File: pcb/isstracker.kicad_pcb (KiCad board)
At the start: 2 copper layers, 18 parts, among them J1 Display, J2 CONTROL, J3 POWER, J4 Error LED, J5 POWER_OUT, Q1 MMBT2222A, Q2 MMBT2222A, U1 CJT1117-5.0

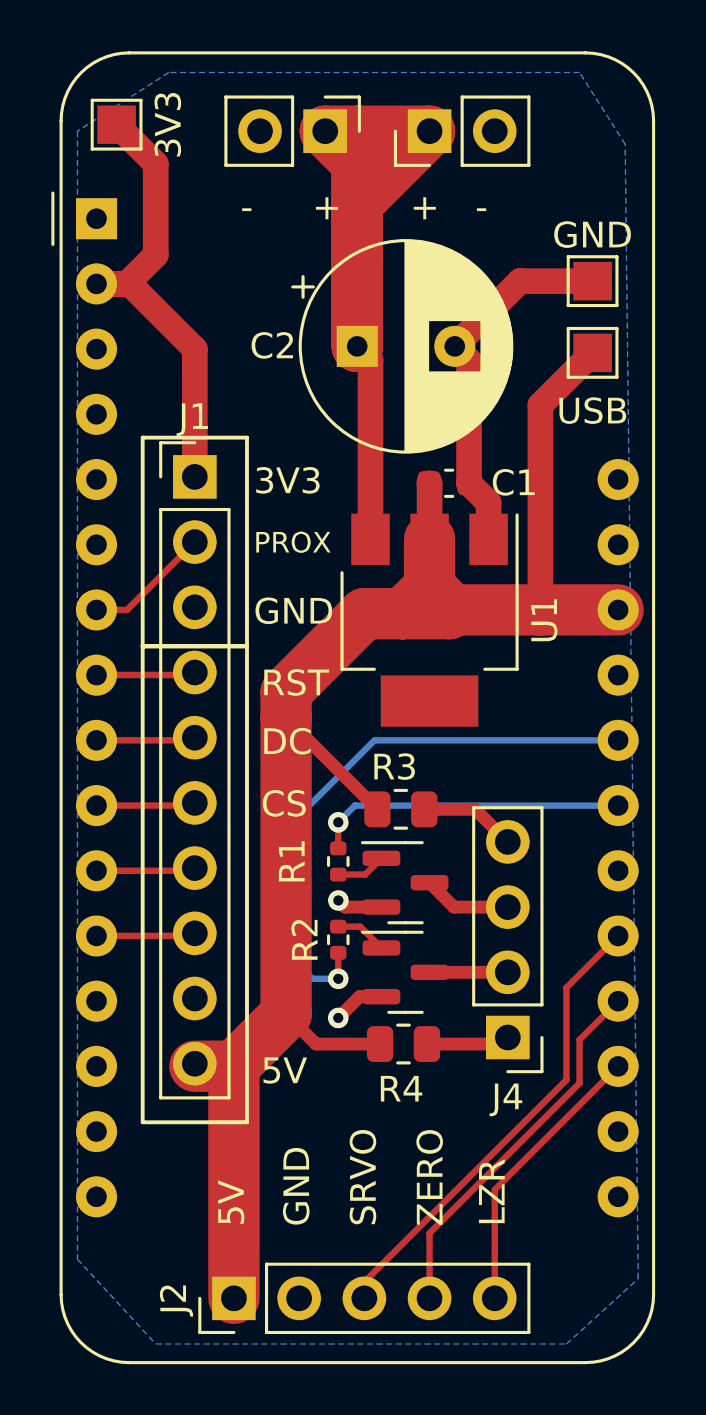
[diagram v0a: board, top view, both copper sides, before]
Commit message: Updating to add internal globe LED control
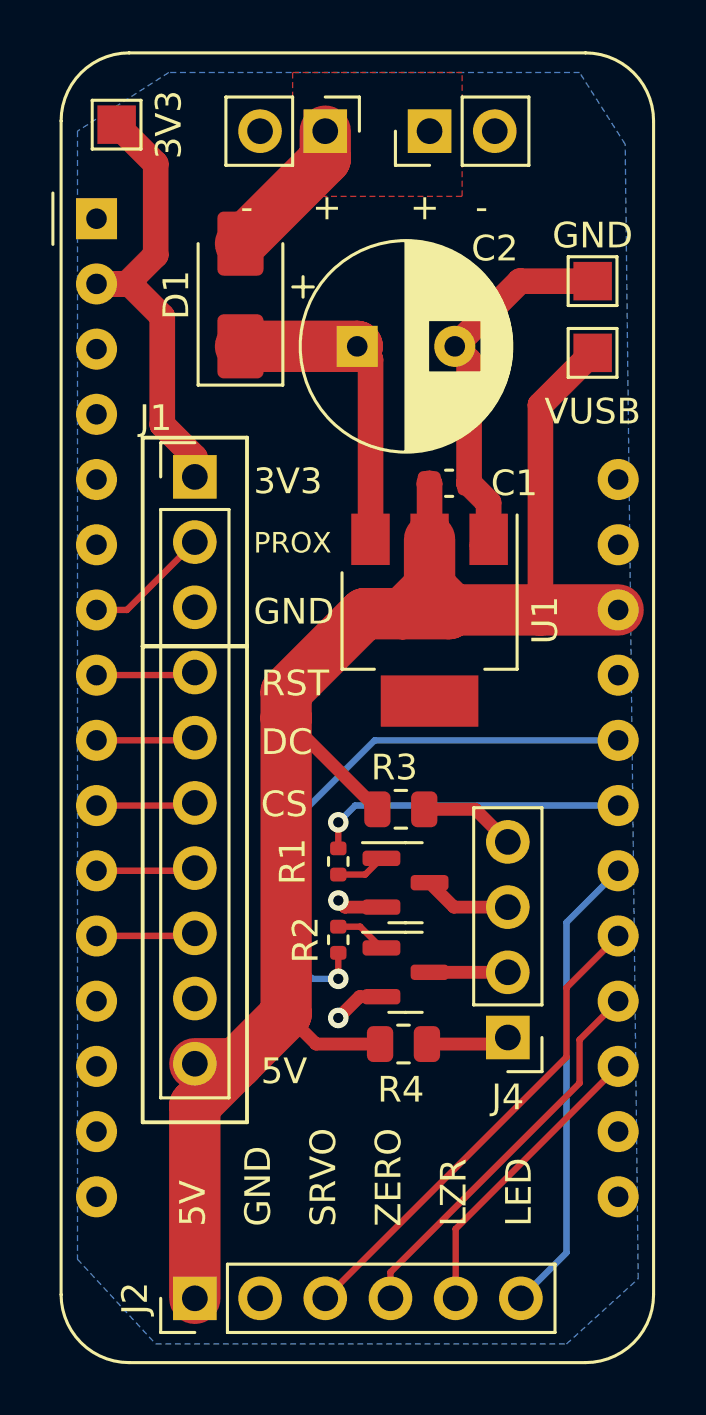
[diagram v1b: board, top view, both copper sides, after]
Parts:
- added D1: D_Schottky, Diode_SMD:D_SMA, F.Cu at (140.2, 72.7)
- J2: value CONTROL -> Control; footprint Connector_PinHeader_2.54mm:PinHeader_1x05_P2.54mm_Vertical -> Connector_PinHeader_2.54mm:PinHeader_1x06_P2.54mm_Vertical
- TP1: value USB -> VUSB
- moved J2 1.52 mm to (138.4, 111.8)
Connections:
- A1 pad 22: unconnected-(A1-D3-Pad22) -> LED
- C2 pad 1: Net-(J3-Pin_1) -> Net-(D1-K)
- J3 pad 1: Net-(J3-Pin_1) -> Net-(D1-A)
- J5 pad 1: Net-(J3-Pin_1) -> Net-(D1-A)
- U1 pad 3: Net-(J3-Pin_1) -> Net-(D1-K)
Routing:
- net Net-(J3-Pin_1): track 38.6 -> 0.00 mm
- net LED: track 0.00 -> 18.4 mm
- net Net-(D1-K): track 0.00 -> 12.3 mm
- net Net-(D1-A): track 0.00 -> 5.75 mm
- net USB: track 67.1 -> 67.9 mm
- net ZERO: track 14.7 -> 15.3 mm
- net LASER: track 11.0 -> 11.7 mm
- net SERVO: track 18.3 -> 18.9 mm
- added copper zone on F.Cu, net Net-(D1-A)
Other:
- board text added: "LED"
